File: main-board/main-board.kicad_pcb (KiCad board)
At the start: 2 copper layers, 100.1 x 67.1 mm, 57 parts, among them J1 Conn_02x08_Odd_Even, J2 7-12V, Q1 2N7000, Q2 2N7000, Q3 2N7000, Q4 2N7000, Q5 2N7000, Q6 2N7000, Q7 2N7000, Q8 2N7000, U1 40106, U2 4024, U3 4040, U4 27C256, U5 LM78L05, U6 ULN2803A, U7 4028, U9 L7805

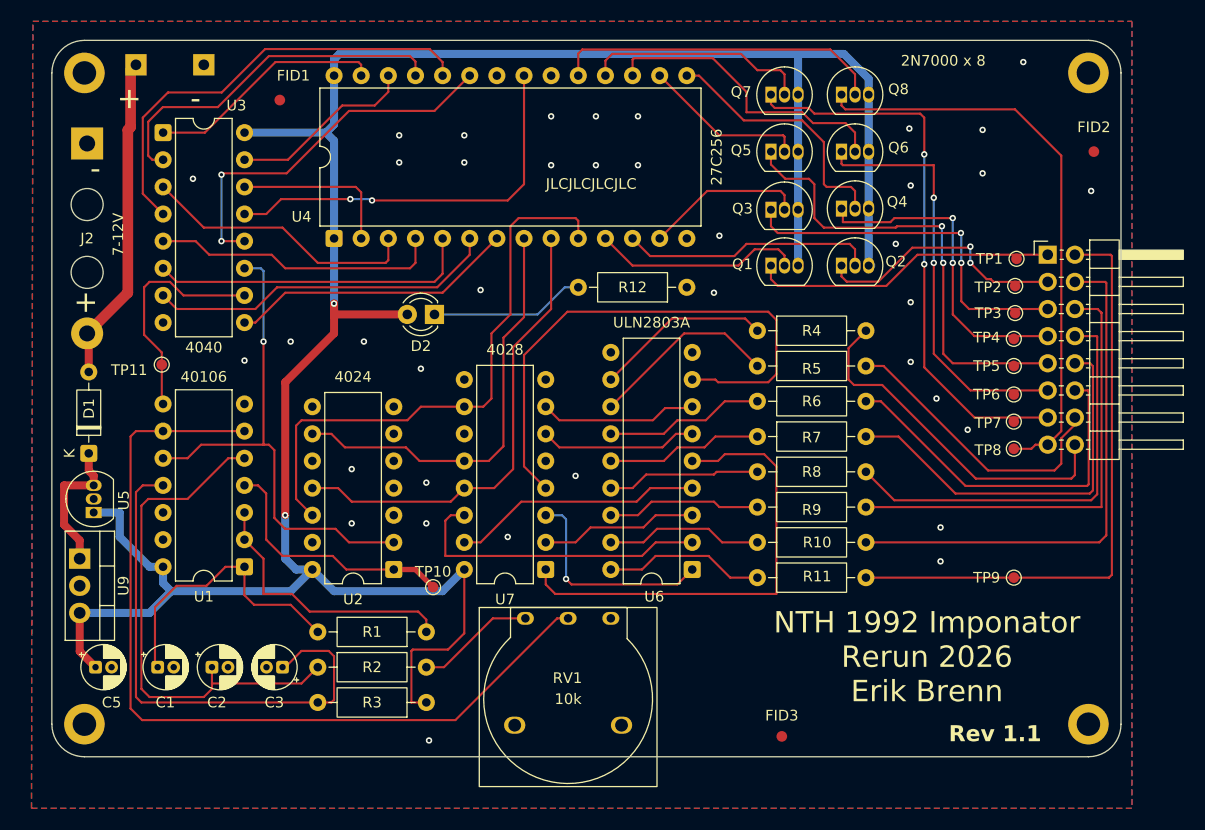
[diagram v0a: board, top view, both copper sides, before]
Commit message: started smd conversion
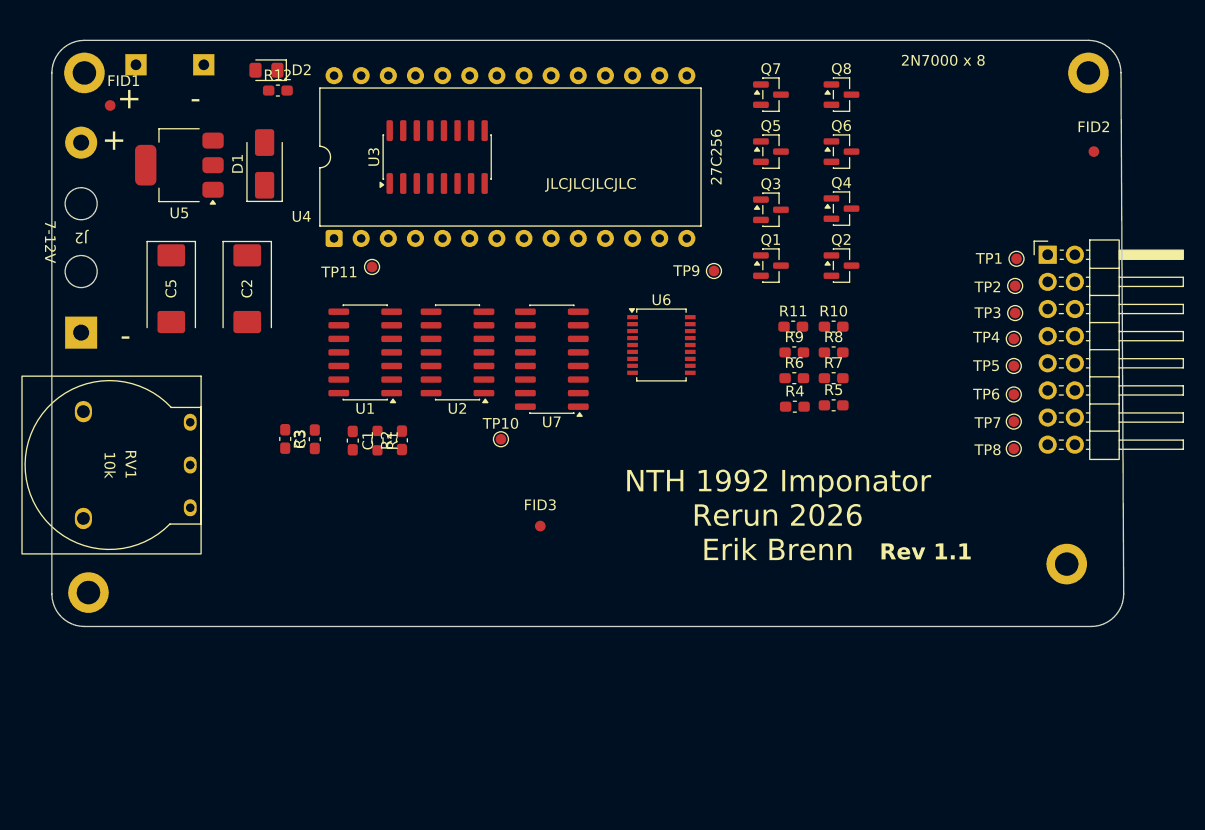
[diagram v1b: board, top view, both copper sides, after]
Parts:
- removed U9: L7805, Package_TO_SOT_THT:TO-220-3_Vertical
- C1: footprint Capacitor_THT:CP_Radial_D4.0mm_P1.50mm -> Capacitor_SMD:C_0603_1608Metric_Pad1.08x0.95mm_HandSolder
- C2: footprint Capacitor_THT:CP_Radial_D4.0mm_P1.50mm -> Capacitor_Tantalum_SMD:CP_EIA-7343-20_Kemet-V
- C3: value 0.1u -> 0.22u; footprint Capacitor_THT:CP_Radial_D4.0mm_P1.50mm -> Capacitor_SMD:C_0603_1608Metric_Pad1.08x0.95mm_HandSolder
- C5: value 0.22u -> 47u; footprint Capacitor_THT:CP_Radial_D4.0mm_P1.50mm -> Capacitor_Tantalum_SMD:CP_EIA-7343-20_Kemet-V
- D1: footprint Diode_THT:D_DO-35_SOD27_P7.62mm_Horizontal -> Diode_SMD:D_SMA
- D2: footprint LED_THT:LED_D3.0mm -> LED_SMD:LED_0805_2012Metric_Pad1.15x1.40mm_HandSolder
- Q1, Q2, Q3, Q4, Q5, Q6, Q7, Q8: value 2N7000 -> AO3400A; footprint Package_TO_SOT_THT:TO-92_Inline -> Package_TO_SOT_SMD:SOT-23
- R1: footprint Resistor_THT:R_Axial_DIN0207_L6.3mm_D2.5mm_P10.16mm_Horizontal -> Resistor_SMD:R_0603_1608Metric_Pad0.98x0.95mm_HandSolder
- R10, R11, R12, R2, R3, R4, R5, R6, R7, R8, R9: footprint Resistor_THT:R_Axial_DIN0207_L6.3mm_D2.5mm_P10.16mm_Horizontal -> Capacitor_SMD:C_0603_1608Metric_Pad1.08x0.95mm_HandSolder
- U1: value 40106 -> CD40106B; footprint Package_DIP:DIP-14_W7.62mm -> Package_SO:SOIC-14_3.9x8.7mm_P1.27mm
- U2: value 4024 -> CD4024B; footprint Package_DIP:DIP-14_W7.62mm -> Package_SO:SOIC-14_3.9x8.7mm_P1.27mm
- U3: value 4040 -> CD4040B; footprint Package_DIP:DIP-16_W7.62mm -> Package_SO:SOIC-16_3.9x9.9mm_P1.27mm
- U5: footprint Package_TO_SOT_THT:TO-92_Inline -> Package_TO_SOT_SMD:SOT-223-3_TabPin2
- U6: footprint Package_DIP:DIP-18_W7.62mm -> Package_SO:SSOP-18_4.4x6.5mm_P0.65mm
- U7: value 4028 -> CD4028B; footprint Package_DIP:DIP-16_W7.62mm -> Package_SO:SOIC-16_3.9x9.9mm_P1.27mm
- moved R12 42.5 mm to (120.7, 62.4), turned to 0 degrees
- moved TP9 40.1 mm to (161.5, 79.2)
- moved RV1 36.3 mm to (112.5, 93.4), turned to -90 degrees
- moved C5 36.1 mm to (110.7, 80.9), turned to -90 degrees
- moved C2 35.6 mm to (117.9, 80.9), turned to -90 degrees
- moved U5 33.5 mm to (111.5, 69.3), turned to 180 degrees
- moved D1 31.7 mm to (119.5, 69.2)
- moved FID3 30.0 mm to (145.3, 103.1)
- moved C1 28.0 mm to (127.7, 95.1), turned to -90 degrees
- moved D2 27.7 mm to (119.7, 60.5)
- moved R3 26.8 mm to (124.2, 95.0), turned to 90 degrees
- moved U3 25.8 mm to (135.6, 68.6), turned to 90 degrees
- moved R11 23.7 mm to (169.0, 84.5)
- moved U1 23.0 mm to (128.9, 86.9)
- moved R2 22.6 mm to (132.3, 95.1), turned to 90 degrees
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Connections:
- Q1 pad 1: Net-(J1-Pin_1) -> Net-(Q1-G)
- Q1 pad 2: Net-(Q1-G) -> Net-(J1-Pin_1)
- Q2 pad 1: Net-(J1-Pin_3) -> Net-(Q2-G)
- Q2 pad 2: Net-(Q2-G) -> Net-(J1-Pin_3)
- Q3 pad 1: Net-(J1-Pin_5) -> Net-(Q3-G)
- Q3 pad 2: Net-(Q3-G) -> Net-(J1-Pin_5)
- Q4 pad 1: Net-(J1-Pin_7) -> Net-(Q4-G)
- Q4 pad 2: Net-(Q4-G) -> Net-(J1-Pin_7)
- Q5 pad 1: Net-(J1-Pin_9) -> Net-(Q5-G)
- Q5 pad 2: Net-(Q5-G) -> Net-(J1-Pin_9)
- Q6 pad 1: Net-(J1-Pin_11) -> Net-(Q6-G)
- Q6 pad 2: Net-(Q6-G) -> Net-(J1-Pin_11)
- Q7 pad 1: Net-(J1-Pin_13) -> Net-(Q7-G)
- Q7 pad 2: Net-(Q7-G) -> Net-(J1-Pin_13)
- Q8 pad 1: Net-(J1-Pin_15) -> Net-(Q8-G)
- Q8 pad 2: Net-(Q8-G) -> Net-(J1-Pin_15)
- U5 pad 1: +5V -> GND
- U5 pad 2: GND -> +5V
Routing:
- net +5V: track 232.1 -> 0.00 mm, vias 2 -> 0
- net Net-(RV1-Pad2): track 81.7 -> 0.00 mm
- net Net-(J1-Pin_2): track 56.5 -> 0.00 mm
- net Net-(J1-Pin_15): track 54.4 -> 0.00 mm
- net Net-(U2-Q0): track 53.6 -> 0.00 mm
- net Net-(J1-Pin_13): track 52.6 -> 0.00 mm, vias 2 -> 0
- net Net-(U6-I8): track 52.3 -> 0.00 mm
- net Net-(C3-Pad1): track 50.6 -> 0.00 mm
- net Net-(J1-Pin_4): track 49.4 -> 0.00 mm
- net Net-(C2-Pad1): track 48.4 -> 0.00 mm
- net Net-(U2-MR): track 47.8 -> 0.00 mm, vias 1 -> 0
- net Net-(U6-I5): track 43.9 -> 0.00 mm
- net Net-(J1-Pin_9): track 43.7 -> 0.00 mm, vias 2 -> 0
- net Net-(U2-Q1): track 43.6 -> 0.00 mm
- net Net-(J1-Pin_6): track 42.9 -> 0.00 mm
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- removed copper zone on B.Cu, net GND
- removed copper zone on F.Cu, net GND
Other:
- board size 100.1 x 67.1 mm -> 100.3 x 54.9 mm

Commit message: docs
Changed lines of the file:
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@@
 	)
 	(gr_text "2N7000 x 8"
-		(at 183.007 59.563 0)
+		(at 179.832 59.182 0)
 		(layer "F.SilkS")
 		(effects
@@
 	)
 	(gr_text "NTH 1992 Imponator\nRerun 2026\nErik Brenn"
-		(at 167.513 106.553 0)
+		(at 168.91 106.172 0)
 		(layer "F.SilkS")
 		(effects
@@
 	)
 	(gr_text "Rev 1.1"
-		(at 177.038 106.426 0)
+		(at 189.484 101.6 0)
 		(layer "F.SilkS")
 		(effects

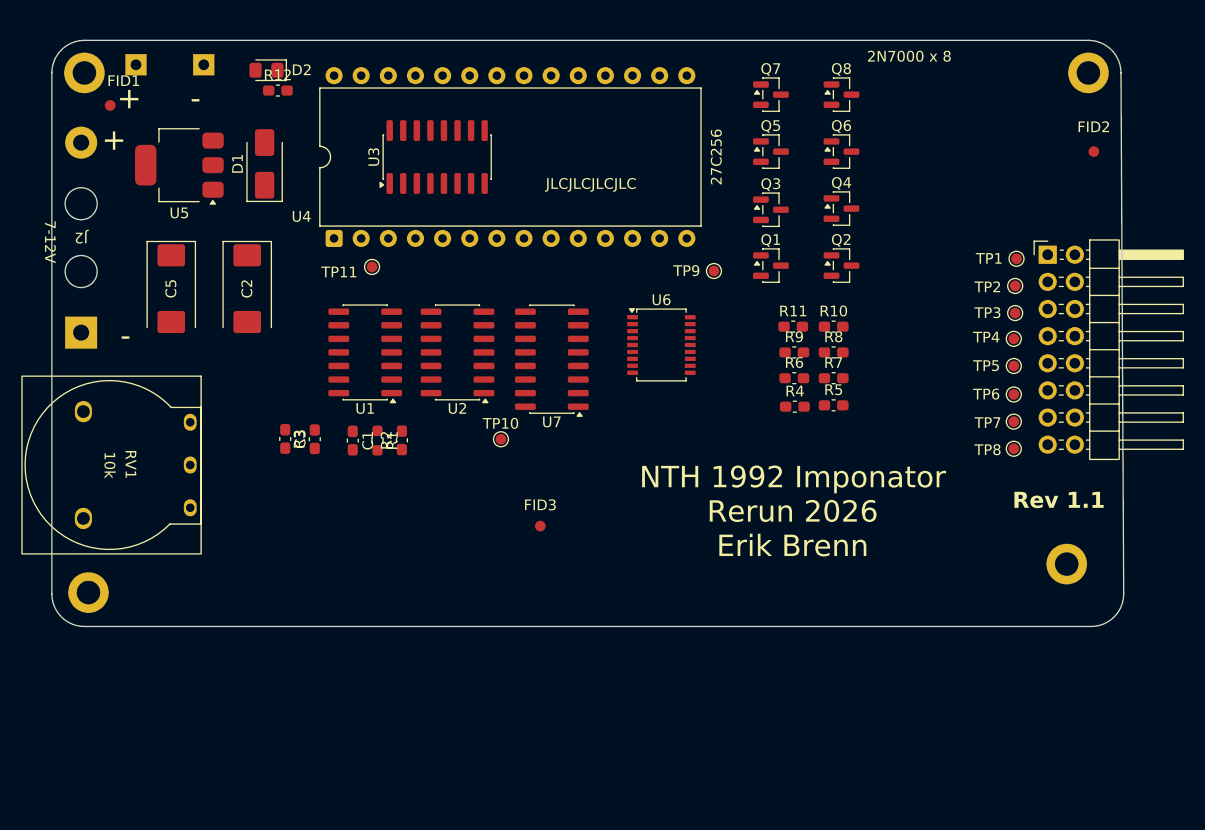
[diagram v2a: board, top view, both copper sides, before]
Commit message: completed routing of smd board
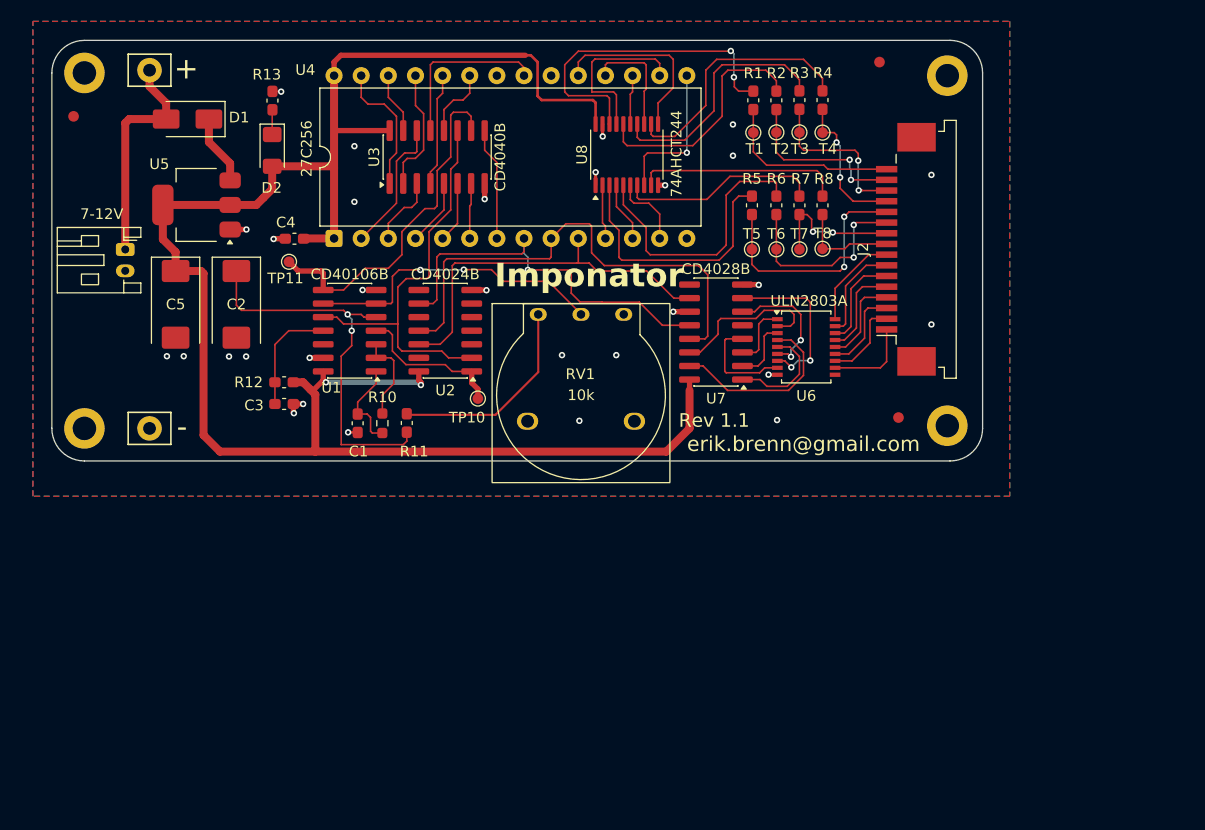
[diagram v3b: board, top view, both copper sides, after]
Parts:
- removed Q1, Q2, Q3, Q4, Q5, Q6, Q7, Q8: AO3400A, Package_TO_SOT_SMD:SOT-23
- removed TP1, TP2, TP3, TP4, TP5, TP6, TP7, TP8, TP9: TestPoint, ezee-footprints:TestPoint_Pad_D1.0mm
- added C4: 0.1u, Capacitor_SMD:C_0603_1608Metric_Pad1.08x0.95mm_HandSolder, F.Cu at (122.3, 76.2)
- added T1: TestPoint, ezee-footprints:TestPoint_Pad_D1.0mm, F.Cu at (165.2, 66.3)
- added T2: TestPoint, ezee-footprints:TestPoint_Pad_D1.0mm, F.Cu at (167.4, 66.3)
- added T3: TestPoint, ezee-footprints:TestPoint_Pad_D1.0mm, F.Cu at (169.5, 66.3)
- added T4: TestPoint, ezee-footprints:TestPoint_Pad_D1.0mm, F.Cu at (171.7, 66.3)
- added T5: TestPoint, ezee-footprints:TestPoint_Pad_D1.0mm, F.Cu at (165.1, 77.2)
- added T6: TestPoint, ezee-footprints:TestPoint_Pad_D1.0mm, F.Cu at (167.4, 77.2)
- added T7: TestPoint, ezee-footprints:TestPoint_Pad_D1.0mm, F.Cu at (169.5, 77.2)
- added T8: TestPoint, ezee-footprints:TestPoint_Pad_D1.0mm, F.Cu at (171.7, 77.2)
- added U8: 74AHCT244, Package_SO:TSSOP-20_4.4x6.5mm_P0.65mm, F.Cu at (153.4, 68.4)
- D1: value 1N4148 -> SS12
- D2: footprint LED_SMD:LED_0805_2012Metric_Pad1.15x1.40mm_HandSolder -> LED_SMD:LED_1206_3216Metric_Pad1.42x1.75mm_HandSolder
- J1: value Conn_02x08_Odd_Even -> 7-12V; footprint Connector_PinHeader_2.54mm:PinHeader_2x08_P2.54mm_Horizontal -> Connector_JST:JST_PH_S2B-PH-K_1x02_P2.00mm_Horizontal
- J2: value 7-12V -> Conn_01x16; footprint ezee-footprints:Battery_Terminals -> Connector_FFC-FPC:TE_1-84952-6_1x16-1MP_P1.0mm_Horizontal
- TPH1, TPH2: footprint ezee-footprints:TestPoint_Hook -> ezee-footprints:LUG_3mm_W4mm
- U5: value LM78L05 -> AMS1117-5.0
- moved J1 86.3 mm to (106.4, 77.2), turned to -90 degrees
- moved J2 77.8 mm to (179.5, 77.2), turned to 90 degrees
- moved FID3 35.0 mm to (178.8, 93.0)
- moved TPH2 34.4 mm to (108.7, 94.0)
- moved RV1 34.1 mm to (145.1, 83.3), turned to 0 degrees
- moved R2 29.0 mm to (167.4, 63.3), turned to 90 degrees
- moved R1 28.9 mm to (165.2, 63.3), turned to 90 degrees
- moved R4 26.1 mm to (171.7, 63.2), turned to 90 degrees
- moved R3 26.0 mm to (169.5, 63.2), turned to 90 degrees
- moved FID2 21.7 mm to (177.0, 59.7), turned to 180 degrees
- moved MH3 17.1 mm to (183.4, 93.7)
- moved R5 15.7 mm to (165.1, 73.1), turned to 90 degrees
- moved U7 15.6 mm to (161.7, 85.0)
- moved MH2 15.4 mm to (102.6, 94.0)
- moved R6 13.9 mm to (167.4, 73.1), turned to 90 degrees
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- renumbered R4 to R1, R1 to R10, R2 to R11, R3 to R12, R12 to R13, R5 to R2, R6 to R3, R7 to R4, R8 to R5, R9 to R6, R10 to R7, R11 to R8
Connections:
- J1 pad 1: Net-(J1-Pin_1) -> Net-(D1-A)
- J1 pad 2: Net-(J1-Pin_2) -> GND
- J2 pad 1: Net-(D1-A) -> Net-(J2-Pin_1)
- J2 pad 2: GND -> Net-(J2-Pin_2)
- R1 pad 1: Net-(U6-O8) -> Net-(J2-Pin_16)
- R1 pad 2: Net-(J1-Pin_16) -> Net-(U8-1Y0)
- R2 pad 1: Net-(U6-O7) -> Net-(J2-Pin_15)
- R2 pad 2: Net-(J1-Pin_14) -> Net-(U8-1Y1)
- R3 pad 1: Net-(U6-O6) -> Net-(J2-Pin_14)
- R3 pad 2: Net-(J1-Pin_12) -> Net-(U8-1Y2)
- R4 pad 1: Net-(U6-O5) -> Net-(J2-Pin_13)
- R4 pad 2: Net-(J1-Pin_10) -> Net-(U8-1Y3)
- R5 pad 1: Net-(U6-O4) -> Net-(J2-Pin_12)
- R5 pad 2: Net-(J1-Pin_8) -> Net-(U8-2Y0)
- R6 pad 1: Net-(U6-O3) -> Net-(J2-Pin_11)
- R6 pad 2: Net-(J1-Pin_6) -> Net-(U8-2Y1)
- R7 pad 1: Net-(U6-O2) -> Net-(J2-Pin_10)
- R7 pad 2: Net-(J1-Pin_4) -> Net-(U8-2Y2)
- R8 pad 1: Net-(U6-O1) -> Net-(J2-Pin_9)
- R8 pad 2: Net-(J1-Pin_2) -> Net-(U8-2Y3)
- U6 pad 11: Net-(U6-O8) -> Net-(J2-Pin_1)
- U6 pad 12: Net-(U6-O7) -> Net-(J2-Pin_2)
- U6 pad 13: Net-(U6-O6) -> Net-(J2-Pin_3)
- U6 pad 14: Net-(U6-O5) -> Net-(J2-Pin_4)
- U6 pad 15: Net-(U6-O4) -> Net-(J2-Pin_5)
- U6 pad 16: Net-(U6-O3) -> Net-(J2-Pin_6)
- U6 pad 17: Net-(U6-O2) -> Net-(J2-Pin_7)
- U6 pad 18: Net-(U6-O1) -> Net-(J2-Pin_8)
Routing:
- net +5V: track 0.00 -> 170.6 mm, vias 0 -> 2
- net Net-(U2-Q1): track 0.00 -> 46.6 mm
- net Net-(U2-MR): track 0.00 -> 38.3 mm
- net Net-(U2-Q2): track 0.00 -> 37.0 mm, vias 0 -> 1
- net Net-(C2-Pad1): track 0.00 -> 36.6 mm, vias 0 -> 2
- net Net-(U2-Q0): track 0.00 -> 35.9 mm
- net Net-(U3-CLK): track 0.00 -> 32.9 mm
- net Net-(U8-1Y0): track 0.00 -> 31.0 mm, vias 0 -> 2
- net Net-(RV1-Pad2): track 0.00 -> 28.6 mm, vias 0 -> 2
- net Net-(U8-2Y1): track 0.00 -> 26.2 mm
- net Net-(U8-2Y0): track 0.00 -> 24.6 mm
- net Net-(U8-1Y3): track 0.00 -> 23.9 mm
- net Net-(U8-1Y2): track 0.00 -> 23.2 mm
- net Net-(U8-1Y1): track 0.00 -> 22.7 mm
- net Net-(J2-Pin_12): track 0.00 -> 22.6 mm, vias 0 -> 2
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- added copper zone on B.Cu, net GND
- added copper zone on F.Cu, net GND
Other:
- board size 100.3 x 54.9 mm -> 87.1 x 39.4 mm
- board text added: "Imponator"
- board text added: "erik.brenn@gmail.com"
- board text removed: "2N7000 x 8"
- board text removed: "JLCJLCJLCJLC"
- board text removed: "NTH 1992 Imponator Rerun 2026 Erik Brenn"
